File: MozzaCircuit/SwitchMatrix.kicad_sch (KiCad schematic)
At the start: 88 parts, among them SW12 SW_ChocV2_rev, SW13 SW_ChocV2_rev, SW15 SW_ChocV2_rev, SW21 SW_ChocV2_rev, SW22 SW_ChocV2_rev, SW23 SW_ChocV2_rev, SW24 SW_ChocV2_rev, SW25 SW_ChocV2_rev, SW31 SW_ChocV2_rev, SW32 SW_ChocV2_rev, SW33 SW_ChocV2_rev, SW34 SW_ChocV2_rev, SW35 SW_ChocV2_rev, SW41 SW_ChocV2_rev, SW42 SW_ChocV2_rev, SW43 SW_ChocV2_rev, SW44 SW_ChocV2_rev, SW51 SW_ChocV2_rev, SW52 SW_ChocV2_rev, SW53 SW_ChocV2_rev, SW54 SW_ChocV2_rev, SW61 SW_ChocV2_rev, SW62 SW_ChocV2_rev, SW63 SW_ChocV2_rev, SW64 SW_ChocV2_rev, SW71 SW_ChocV2_rev, SW72 SW_ChocV2_rev, SW73 SW_ChocV2_rev, SW82 SW_ChocV2_rev, SW83 SW_ChocV2_rev, SW84 SW_ChocV2_rev

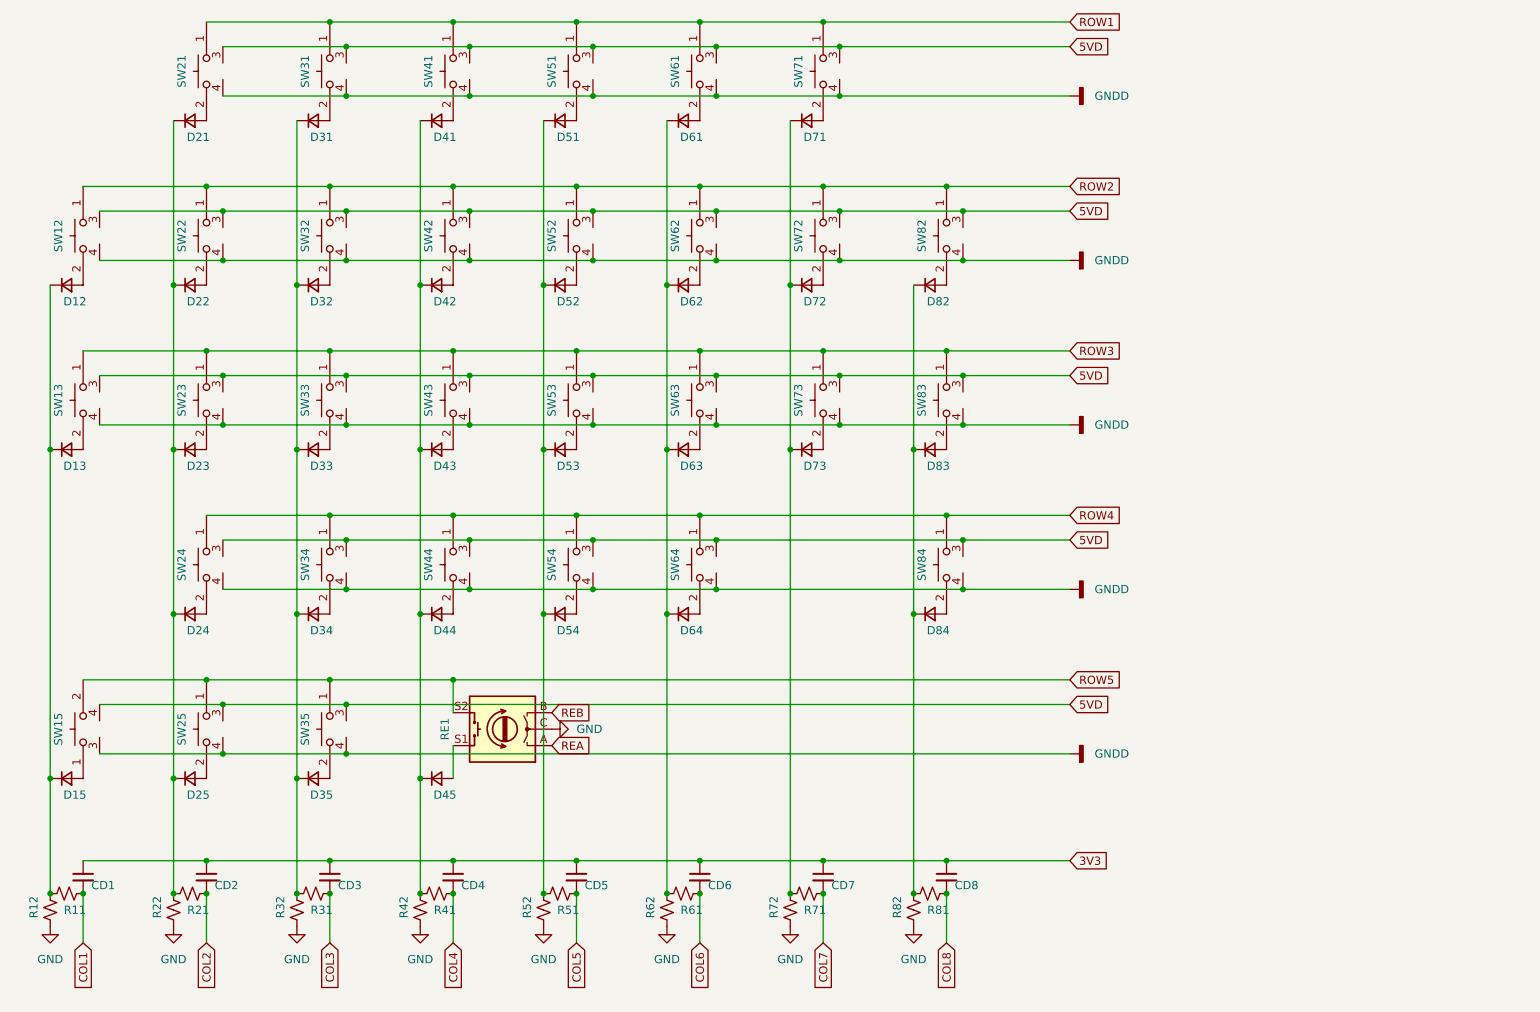
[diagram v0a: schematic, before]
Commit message: added 3D models, debounce for encoder
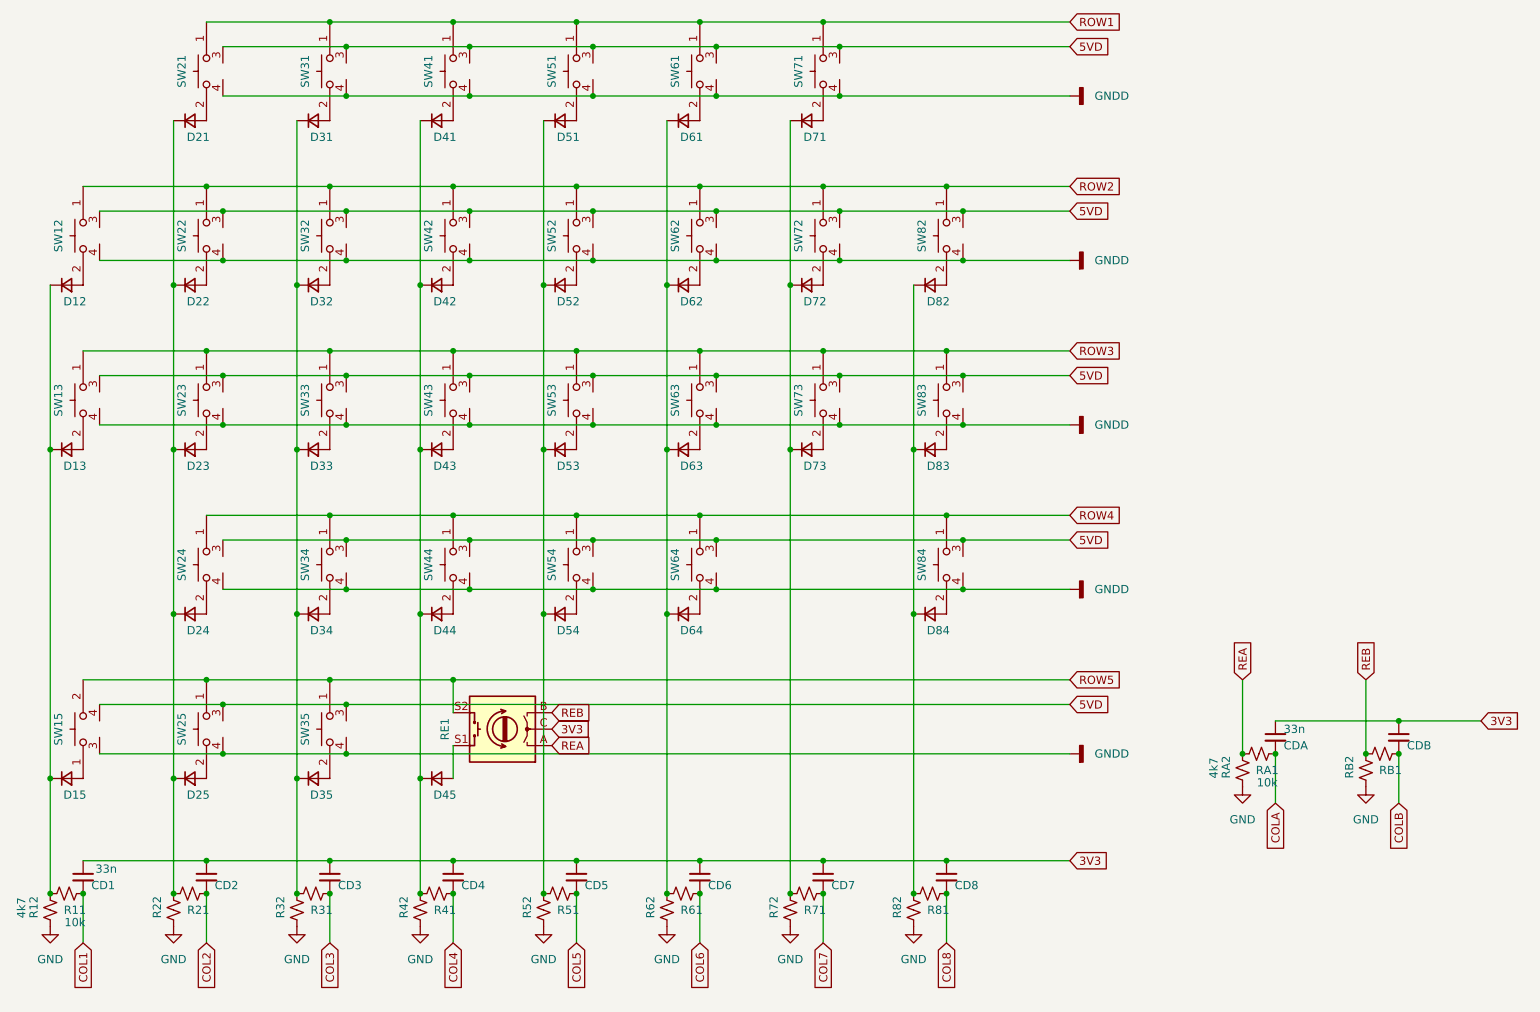
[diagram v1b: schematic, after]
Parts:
- added CDA: 33n, 00_KeyParts:C_2012_rev, symbol Device:C_Small
- added CDB: C_Small, 00_KeyParts:C_2012_rev, symbol Device:C_Small
- added RA1: 10k, 00_KeyParts:R_2012_rev, symbol Device:R_Small_US
- added RA2: 4k7, 00_KeyParts:R_2012_rev, symbol Device:R_Small_US
- added RB1, RB2: R_Small_US, 00_KeyParts:R_2012_rev, symbol Device:R_Small_US
- CD1: value C_Small -> 33n; footprint (none) -> 00_KeyParts:C_2012_rev
- CD2, CD3, CD4, CD5, CD6, CD7, CD8: footprint (none) -> 00_KeyParts:C_2012_rev
- D12, D13, D15, D21, D22, D23, D24, D25, D31, D32, D33, D34, D35, D41, D42, D43, D44, D45, D51, D52, D53, D54, D61, D62, D63, D64, D71, D72, D73, D82, D83, D84: footprint (none) -> 00_KeyParts:D_SOD-323_both_sides
- R11: value R_Small_US -> 10k; footprint (none) -> 00_KeyParts:R_2012_rev
- R12: value R_Small_US -> 4k7; footprint (none) -> 00_KeyParts:R_2012_rev
- R21, R22, R31, R32, R41, R42, R51, R52, R61, R62, R71, R72, R81, R82: footprint (none) -> 00_KeyParts:R_2012_rev
- RE1: footprint (none) -> 00_KeyParts:RotaryEncoder_Bourns_PEC12R-4215F
- SW12, SW13, SW15, SW21, SW22, SW23, SW24, SW25, SW31, SW32, SW33, SW34, SW35, SW41, SW42, SW43, SW44, SW51, SW52, SW53, SW54, SW61, SW62, SW63, SW64, SW71, SW72, SW73, SW82, SW83, SW84: footprint (none) -> 00_KeyParts:ChocV2_rev
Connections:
- net 3V3: now also RE1.C, CDA.1, CDB.1
- net GND: now also RA2.2, RB2.2; no longer RE1.C
- net REA: now also RA1.1, RA2.1
- net REB: now also RB1.1, RB2.1
- new net COLA: CDA.2, RA1.2
- new net COLB: CDB.2, RB1.2

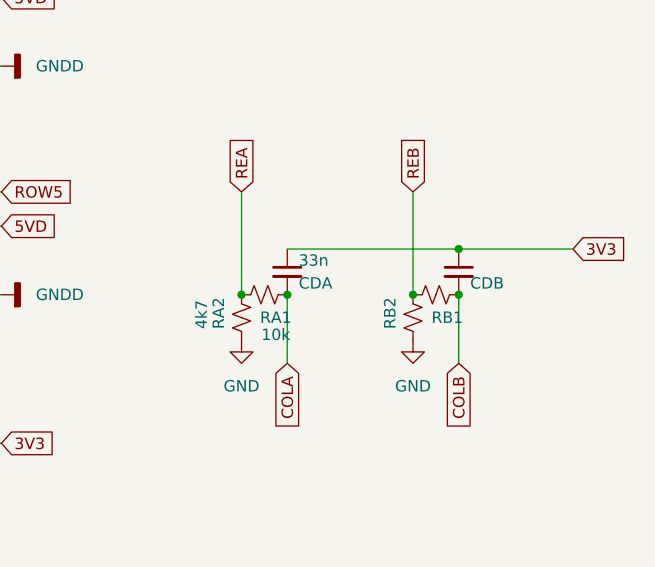
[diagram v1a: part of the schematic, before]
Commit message: added qfn footprints
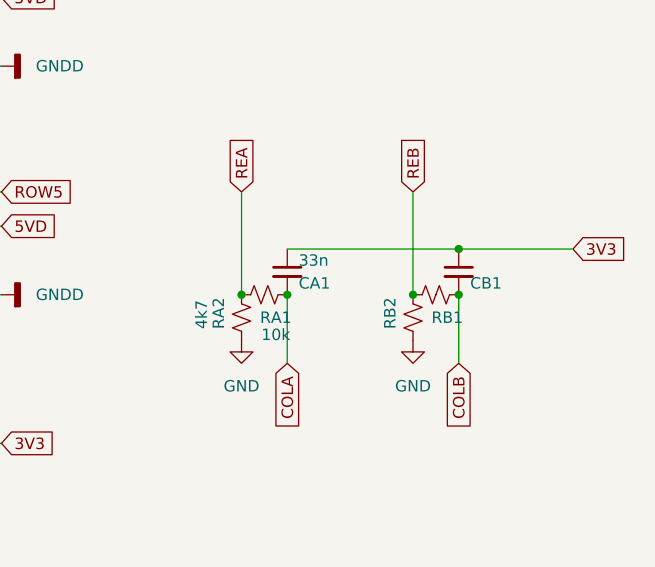
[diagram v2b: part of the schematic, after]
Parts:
- renumbered CDA to CA1, CDB to CB1
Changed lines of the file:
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@@
   (symbol (lib_id "power:GND") (at 210.82 143.51 0) (unit 1)
     (in_bom yes) (on_board yes) (fields_autoplaced)
-    (property "Reference" "#PWR?" (id 0) (at 210.82 149.86 0)
+    (property "Reference" "#PWR0137" (id 0) (at 210.82 149.86 0)
       (effects (font (size 1.27 1.27)) hide)
     )
@@
   (symbol (lib_id "Device:C_Small") (at 215.9 135.89 0) (unit 1)
     (in_bom yes) (on_board yes)
-    (property "Reference" "CDA" (id 0) (at 217.17 137.16 0)
+    (property "Reference" "CA1" (id 0) (at 217.17 137.16 0)
       (effects (font (size 1.27 1.27)) (justify left))
     )
@@
   (symbol (lib_id "power:GND") (at 229.87 143.51 0) (unit 1)
     (in_bom yes) (on_board yes) (fields_autoplaced)
-    (property "Reference" "#PWR?" (id 0) (at 229.87 149.86 0)
+    (property "Reference" "#PWR0122" (id 0) (at 229.87 149.86 0)
       (effects (font (size 1.27 1.27)) hide)
     )
@@
   (symbol (lib_id "Device:C_Small") (at 234.95 135.89 0) (unit 1)
     (in_bom yes) (on_board yes)
-    (property "Reference" "CDB" (id 0) (at 236.22 137.16 0)
-      (effects (font (size 1.27 1.27)) (justify left))
-    )
+    (property "Reference" "CB1" (id 0) (at 236.22 137.16 0)
+      (effects (font (size 1.27 1.27)) (justify left))
+    )

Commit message: started place and route
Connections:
- net 5VD: now also SW12.4, SW13.4, SW15.5, SW21.4, SW22.4, SW23.4, SW24.4, SW25.4, SW31.4, SW32.4, SW33.4, SW34.4, SW35.4, SW41.4, SW42.4, SW43.4, SW44.4, SW51.4, SW52.4, SW53.4, SW54.4, SW61.4, SW62.4, SW63.4, SW64.4, SW71.4, SW72.4, SW73.4, SW82.4, SW83.4, SW84.4; no longer SW12.3, SW13.3, SW15.4, SW21.3, SW22.3, SW23.3, SW24.3, SW25.3, SW31.3, SW32.3, SW33.3, SW34.3, SW35.3, SW41.3, SW42.3, SW43.3, SW44.3, SW51.3, SW52.3, SW53.3, SW54.3, SW61.3, SW62.3, SW63.3, SW64.3, SW71.3, SW72.3, SW73.3, SW82.3, SW83.3, SW84.3
- net GNDD: now also SW12.5, SW13.5, SW15.4, SW21.5, SW22.5, SW23.5, SW24.5, SW25.5, SW31.5, SW32.5, SW33.5, SW34.5, SW35.5, SW41.5, SW42.5, SW43.5, SW44.5, SW51.5, SW52.5, SW53.5, SW54.5, SW61.5, SW62.5, SW63.5, SW64.5, SW71.5, SW72.5, SW73.5, SW82.5, SW83.5, SW84.5; no longer SW12.4, SW13.4, SW15.3, SW21.4, SW22.4, SW23.4, SW24.4, SW25.4, SW31.4, SW32.4, SW33.4, SW34.4, SW35.4, SW41.4, SW42.4, SW43.4, SW44.4, SW51.4, SW52.4, SW53.4, SW54.4, SW61.4, SW62.4, SW63.4, SW64.4, SW71.4, SW72.4, SW73.4, SW82.4, SW83.4, SW84.4
- net ROW5: now also SW15.3
- net at D23.2 (A), SW23.2: now also SW23.3
- net at D54.2 (A), SW54.2: now also SW54.3
- net at D22.2 (A), SW22.2: now also SW22.3
- net at D44.2 (A), SW44.2: now also SW44.3
- net at D34.2 (A), SW34.2: now also SW34.3
- net at D35.2 (A), SW35.2: now also SW35.3
- net at D21.2 (A), SW21.2: now also SW21.3
- net at D42.2 (A), SW42.2: now also SW42.3
- net at D24.2 (A), SW24.2: now also SW24.3
- net at D13.2 (A), SW13.2: now also SW13.3
- net at D32.2 (A), SW32.2: now also SW32.3
- net at D72.2 (A), SW72.2: now also SW72.3
- net at D53.2 (A), SW53.2: now also SW53.3
- net at D73.2 (A), SW73.2: now also SW73.3
- net at D41.2 (A), SW41.2: now also SW41.3
- net at D43.2 (A), SW43.2: now also SW43.3
- net at D83.2 (A), SW83.2: now also SW83.3
- net at D52.2 (A), SW52.2: now also SW52.3
- net at D12.2 (A), SW12.2: now also SW12.3
- net at D62.2 (A), SW62.2: now also SW62.3
- net at D63.2 (A), SW63.2: now also SW63.3
- net at D71.2 (A), SW71.2: now also SW71.3
- net at D33.2 (A), SW33.2: now also SW33.3
- net at D51.2 (A), SW51.2: now also SW51.3
- net at D61.2 (A), SW61.2: now also SW61.3
- net at D25.2 (A), SW25.2: now also SW25.3
- net at D84.2 (A), SW84.2: now also SW84.3
- net at D64.2 (A), SW64.2: now also SW64.3
- net at D31.2 (A), SW31.2: now also SW31.3
- net at D82.2 (A), SW82.2: now also SW82.3

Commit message: led direction
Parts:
- renumbered D12 to D14, SW12 to SW14
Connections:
- net 5VD: no longer SW14.4
- net GNDD: no longer SW14.5
- net ROW2: no longer SW14.1
- net ROW4: now also SW14.1
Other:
- moved on the sheet: D14, SW14
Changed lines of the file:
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@@
   (junction (at 69.85 50.8) (diameter 0) (color 0 0 0 0)
   )
+  (junction (at 26.67 116.84) (diameter 0) (color 0 0 0 0)
+  )
   (junction (at 129.54 80.01) (diameter 0) (color 0 0 0 0)
   )
@@
   (junction (at 72.39 113.03) (diameter 0) (color 0 0 0 0)
   )
-  (junction (at 26.67 91.44) (diameter 0) (color 0 0 0 0)
-  )
   (junction (at 88.9 127) (diameter 0) (color 0 0 0 0)
   )
@@
   (junction (at 69.85 154.94) (diameter 0) (color 0 0 0 0)
   )
-  (junction (at 53.34 62.23) (diameter 0) (color 0 0 0 0)
-  )
   (junction (at 72.39 36.83) (diameter 0) (color 0 0 0 0)
   )
@@
   (junction (at 88.9 160.02) (diameter 0) (color 0 0 0 0)
   )
+  (junction (at 50.8 101.6) (diameter 0) (color 0 0 0 0)
+  )
   (junction (at 72.39 54.61) (diameter 0) (color 0 0 0 0)
   )
@@
   (junction (at 167.64 113.03) (diameter 0) (color 0 0 0 0)
   )
-  (junction (at 50.8 50.8) (diameter 0) (color 0 0 0 0)
-  )
   (junction (at 107.95 101.6) (diameter 0) (color 0 0 0 0)
   )
@@
   (junction (at 72.39 80.01) (diameter 0) (color 0 0 0 0)
   )
-  (junction (at 53.34 54.61) (diameter 0) (color 0 0 0 0)
-  )
   (junction (at 146.05 25.4) (diameter 0) (color 0 0 0 0)
   )
@@
     (stroke (width 0) (type default) (color 0 0 0 0))
   )
-  (wire (pts (xy 26.67 66.04) (xy 26.67 91.44))
-    (stroke (width 0) (type default) (color 0 0 0 0))
-  )
   (wire (pts (xy 167.64 87.63) (xy 184.15 87.63))
     (stroke (width 0) (type default) (color 0 0 0 0))
@@
     (stroke (width 0) (type default) (color 0 0 0 0))
   )
+  (wire (pts (xy 26.67 116.84) (xy 26.67 142.24))
+    (stroke (width 0) (type default) (color 0 0 0 0))
+  )
   (wire (pts (xy 165.1 160.02) (xy 165.1 167.64))
     (stroke (width 0) (type default) (color 0 0 0 0))
@@
     (stroke (width 0) (type default) (color 0 0 0 0))
   )
-  (wire (pts (xy 34.29 54.61) (xy 53.34 54.61))
-    (stroke (width 0) (type default) (color 0 0 0 0))
-  )
   (wire (pts (xy 165.1 154.94) (xy 184.15 154.94))
     (stroke (width 0) (type default) (color 0 0 0 0))
@@
     (stroke (width 0) (type default) (color 0 0 0 0))
   )
+  (wire (pts (xy 31.75 101.6) (xy 50.8 101.6))
+    (stroke (width 0) (type default) (color 0 0 0 0))
+  )
   (wire (pts (xy 102.87 91.44) (xy 102.87 116.84))
     (stroke (width 0) (type default) (color 0 0 0 0))
@@
     (stroke (width 0) (type default) (color 0 0 0 0))
   )
-  (wire (pts (xy 31.75 50.8) (xy 50.8 50.8))
-    (stroke (width 0) (type default) (color 0 0 0 0))
-  )
   (wire (pts (xy 165.1 101.6) (xy 184.15 101.6))
     (stroke (width 0) (type default) (color 0 0 0 0))
@@
     (stroke (width 0) (type default) (color 0 0 0 0))
   )
-  (wire (pts (xy 26.67 91.44) (xy 26.67 142.24))
+  (wire (pts (xy 26.67 91.44) (xy 26.67 116.84))
     (stroke (width 0) (type default) (color 0 0 0 0))
   )
@@
   )
   (wire (pts (xy 215.9 133.35) (xy 234.95 133.35))
-    (stroke (width 0) (type default) (color 0 0 0 0))
-  )
-  (wire (pts (xy 34.29 62.23) (xy 53.34 62.23))
     (stroke (width 0) (type default) (color 0 0 0 0))
   )
@@
     (pin "2")
   )
-  (symbol (lib_name "SW_ChocV2_rev_15") (lib_id "00_KeyParts:SW_ChocV2_rev") (at 31.75 58.42 90) (mirror x) (unit 1)
-    (in_bom yes) (on_board yes)
-    (property "Reference" "SW12" (id 0) (at 27.94 58.42 0))
-    (property "Value" "SW_ChocV2_rev" (id 1) (at 27.178 58.42 0)
-      (effects (font (size 1.27 1.27)) hide)
-    )
-    (property "Footprint" "00_KeyParts:ChocV2_rev" (id 2) (at 31.75 58.42 0)
-      (effects (font (size 1.27 1.27)) hide)
-    )
-    (property "Datasheet" "" (id 3) (at 31.75 58.42 0)
+  (symbol (lib_name "SW_ChocV2_rev_15") (lib_id "00_KeyParts:SW_ChocV2_rev") (at 31.75 109.22 90) (mirror x) (unit 1)
+    (in_bom yes) (on_board yes)
+    (property "Reference" "SW14" (id 0) (at 27.94 109.22 0))
+    (property "Value" "SW_ChocV2_rev" (id 1) (at 27.178 109.22 0)
+      (effects (font (size 1.27 1.27)) hide)
+    )
+    (property "Footprint" "00_KeyParts:ChocV2_rev" (id 2) (at 31.75 109.22 0)
+      (effects (font (size 1.27 1.27)) hide)
+    )
+    (property "Datasheet" "" (id 3) (at 31.75 109.22 0)
       (effects (font (size 1.27 1.27)) hide)
     )
@@
     (pin "1")
   )
-  (symbol (lib_id "Device:D_Small") (at 29.21 66.04 0) (unit 1)
-    (in_bom yes) (on_board yes)
-    (property "Reference" "D12" (id 0) (at 30.48 68.58 0))
-    (property "Value" "D_Small" (id 1) (at 29.21 62.23 0)
-      (effects (font (size 1.27 1.27)) hide)
-    )
-    (property "Footprint" "00_KeyParts:D_SOD-323_both_sides" (id 2) (at 29.21 66.04 90)
-      (effects (font (size 1.27 1.27)) hide)
-    )
-    (property "Datasheet" "~" (id 3) (at 29.21 66.04 90)
-      (effects (font (size 1.27 1.27)) hide)
-    )
+  (symbol (lib_id "Device:D_Small") (at 29.21 116.84 0) (unit 1)
+    (in_bom yes) (on_board yes)
+    (property "Reference" "D14" (id 0) (at 30.48 119.38 0))
+    (property "Value" "D_Small" (id 1) (at 29.21 113.03 0)
+      (effects (font (size 1.27 1.27)) hide)
+    )
+    (property "Footprint" "00_KeyParts:D_SOD-323_both_sides" (id 2) (at 29.21 116.84 90)
+      (effects (font (size 1.27 1.27)) hide)
+    )
+    (property "Datasheet" "~" (id 3) (at 29.21 116.84 90)
+      (effects (font (size 1.27 1.27)) hide)
+    )

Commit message: 1608 R&C
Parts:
- CA1, CB1, CD1, CD2, CD3, CD4, CD5, CD6, CD7, CD8: footprint 00_KeyParts:C_2012_rev -> 00_KeyParts:C_1608_HandSolder_both_sides
- R11, R12, R21, R22, R31, R32, R41, R42, R51, R52, R61, R62, R71, R72, R81, R82, RA1, RA2, RB1, RB2: footprint 00_KeyParts:R_2012_rev -> 00_KeyParts:R_1608_HandSolder_both_sides
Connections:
- net 5VD: now also SW13.5, SW23.5, SW31.5, SW33.5, SW41.5, SW43.5, SW51.5, SW53.5, SW61.5, SW63.5, SW71.5, SW73.5, SW83.5; no longer SW13.4, SW21.4, SW23.4, SW31.4, SW33.4, SW41.4, SW43.4, SW51.4, SW53.4, SW61.4, SW63.4, SW71.4, SW73.4, SW83.4
- net GNDD: now also SW13.4, SW21.4, SW23.4, SW31.4, SW33.4, SW41.4, SW43.4, SW51.4, SW53.4, SW61.4, SW63.4, SW71.4, SW73.4, SW83.4; no longer SW13.5, SW21.5, SW23.5, SW31.5, SW33.5, SW41.5, SW43.5, SW51.5, SW53.5, SW61.5, SW63.5, SW71.5, SW73.5, SW83.5
- new net 4V3D: SW21.5

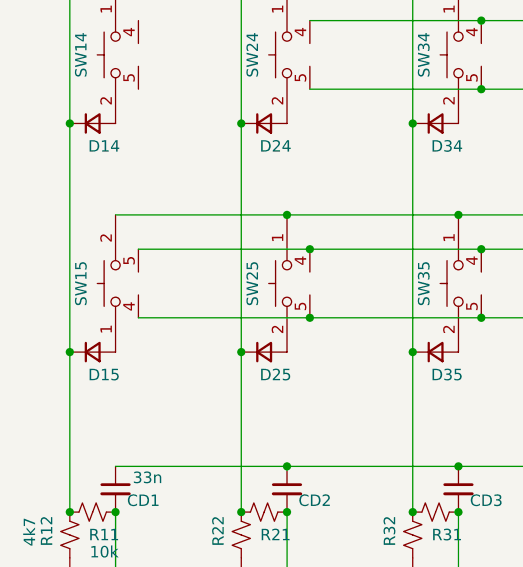
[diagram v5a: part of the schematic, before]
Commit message: led wiring, fix fp silk overlaps
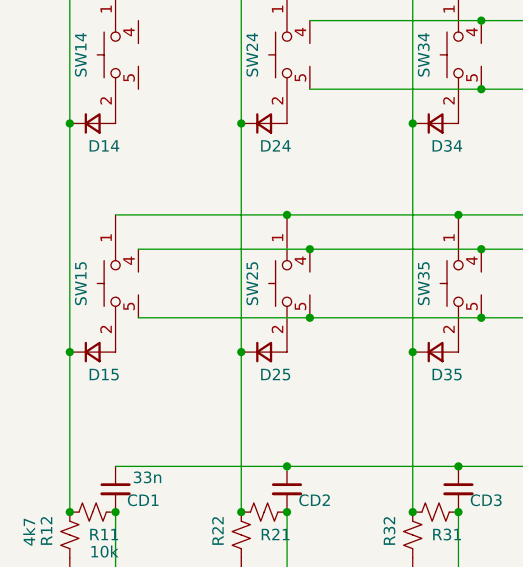
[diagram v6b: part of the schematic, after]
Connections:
- net 5VD: now also SW15.4; no longer SW15.5
- net GNDD: now also SW15.5; no longer SW15.4
- net ROW5: now also SW15.1; no longer SW15.2, SW15.3
- net at D15.2 (A): now also SW15.2, SW15.3; no longer SW15.1
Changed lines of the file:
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@@
     (pin "2")
   )
-  (symbol (lib_name "SW_ChocV2_rev_23") (lib_id "00_KeyParts:SW_ChocV2_rev") (at 31.75 134.62 90) (unit 1)
+  (symbol (lib_name "SW_ChocV2_rev_23") (lib_id "00_KeyParts:SW_ChocV2_rev") (at 31.75 134.62 90) (mirror x) (unit 1)
     (in_bom yes) (on_board yes)
     (property "Reference" "SW15" (id 0) (at 27.94 134.62 0))
